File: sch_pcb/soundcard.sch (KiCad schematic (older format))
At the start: 52 parts, among them J501 MicroUSB, U501 CM108B, U502 CM108B, U503 TUSB2036, Y501 6MHz

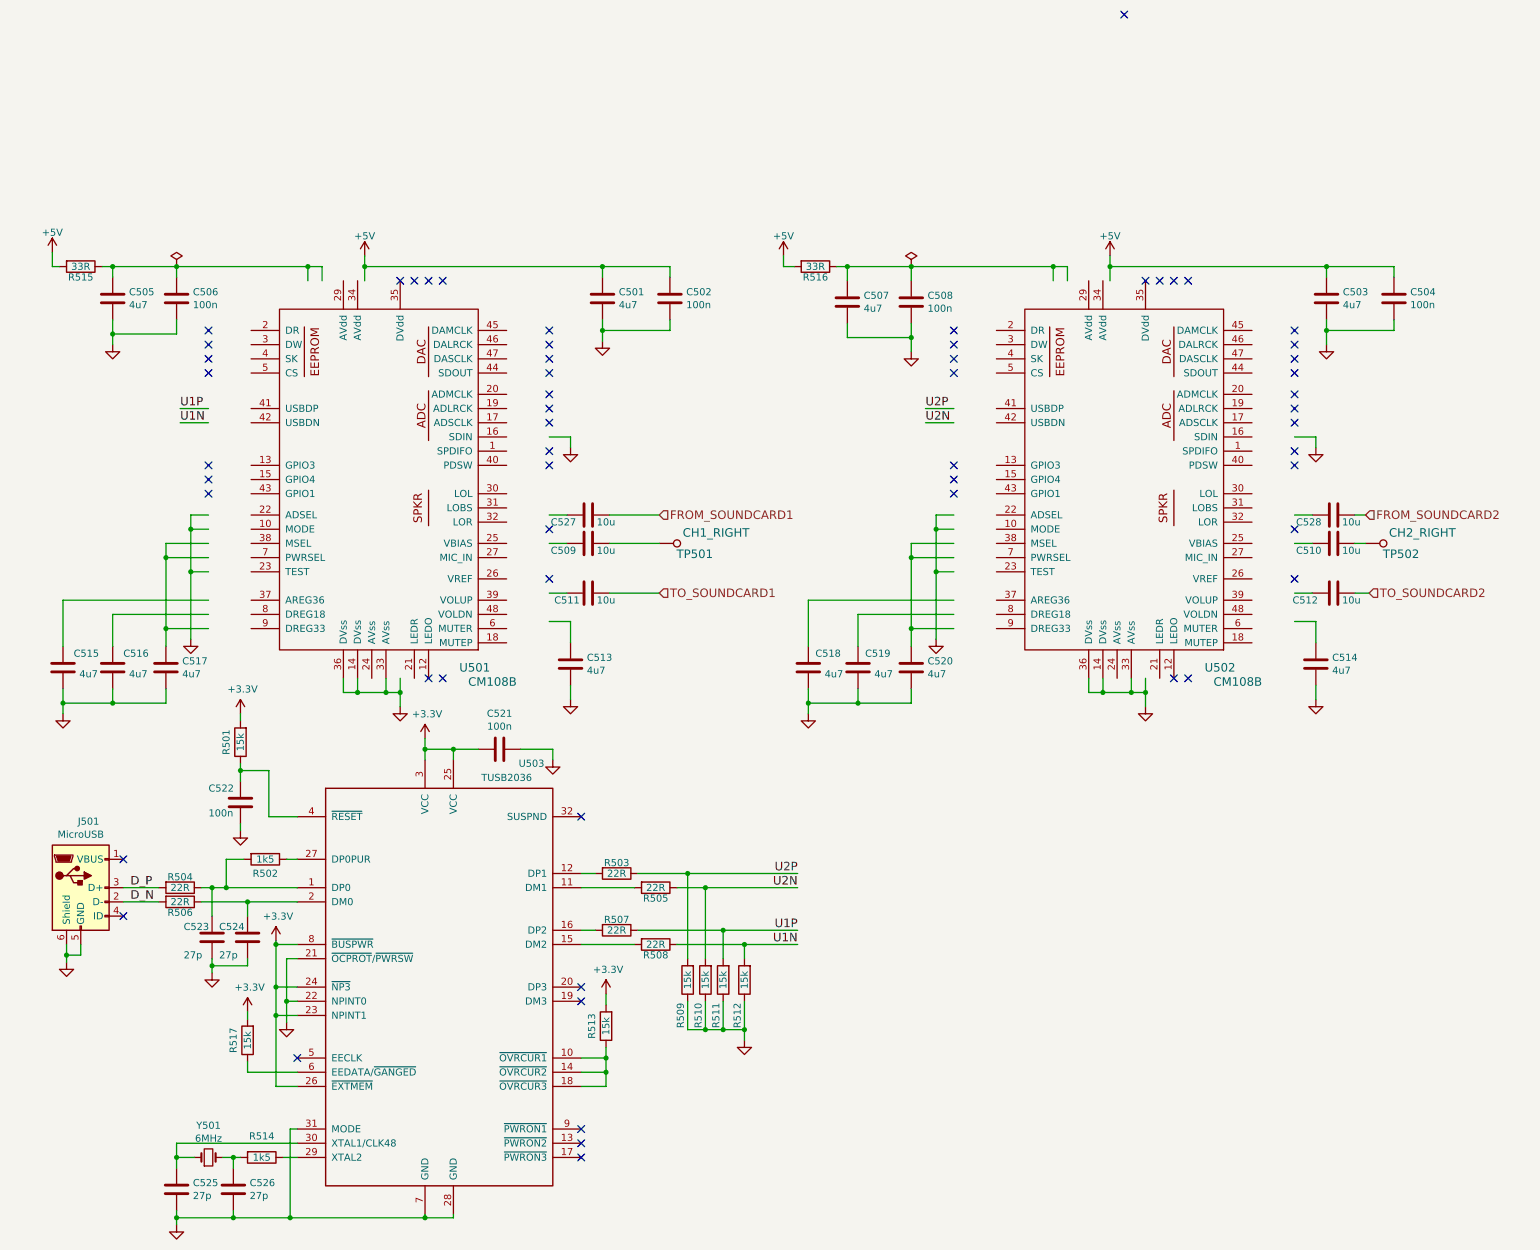
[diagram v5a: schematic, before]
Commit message: Add files via upload
Add a PMOS switch to allow turning on the soundcard section (hub and 2 soundcard chips) after the Pi has booted.  For some reason, doing so before the desktop loads causes it to hang..
Change gain resistors in opamp stages to move the sweet spot closer to the center of the digital pots to allow for more adjustment range
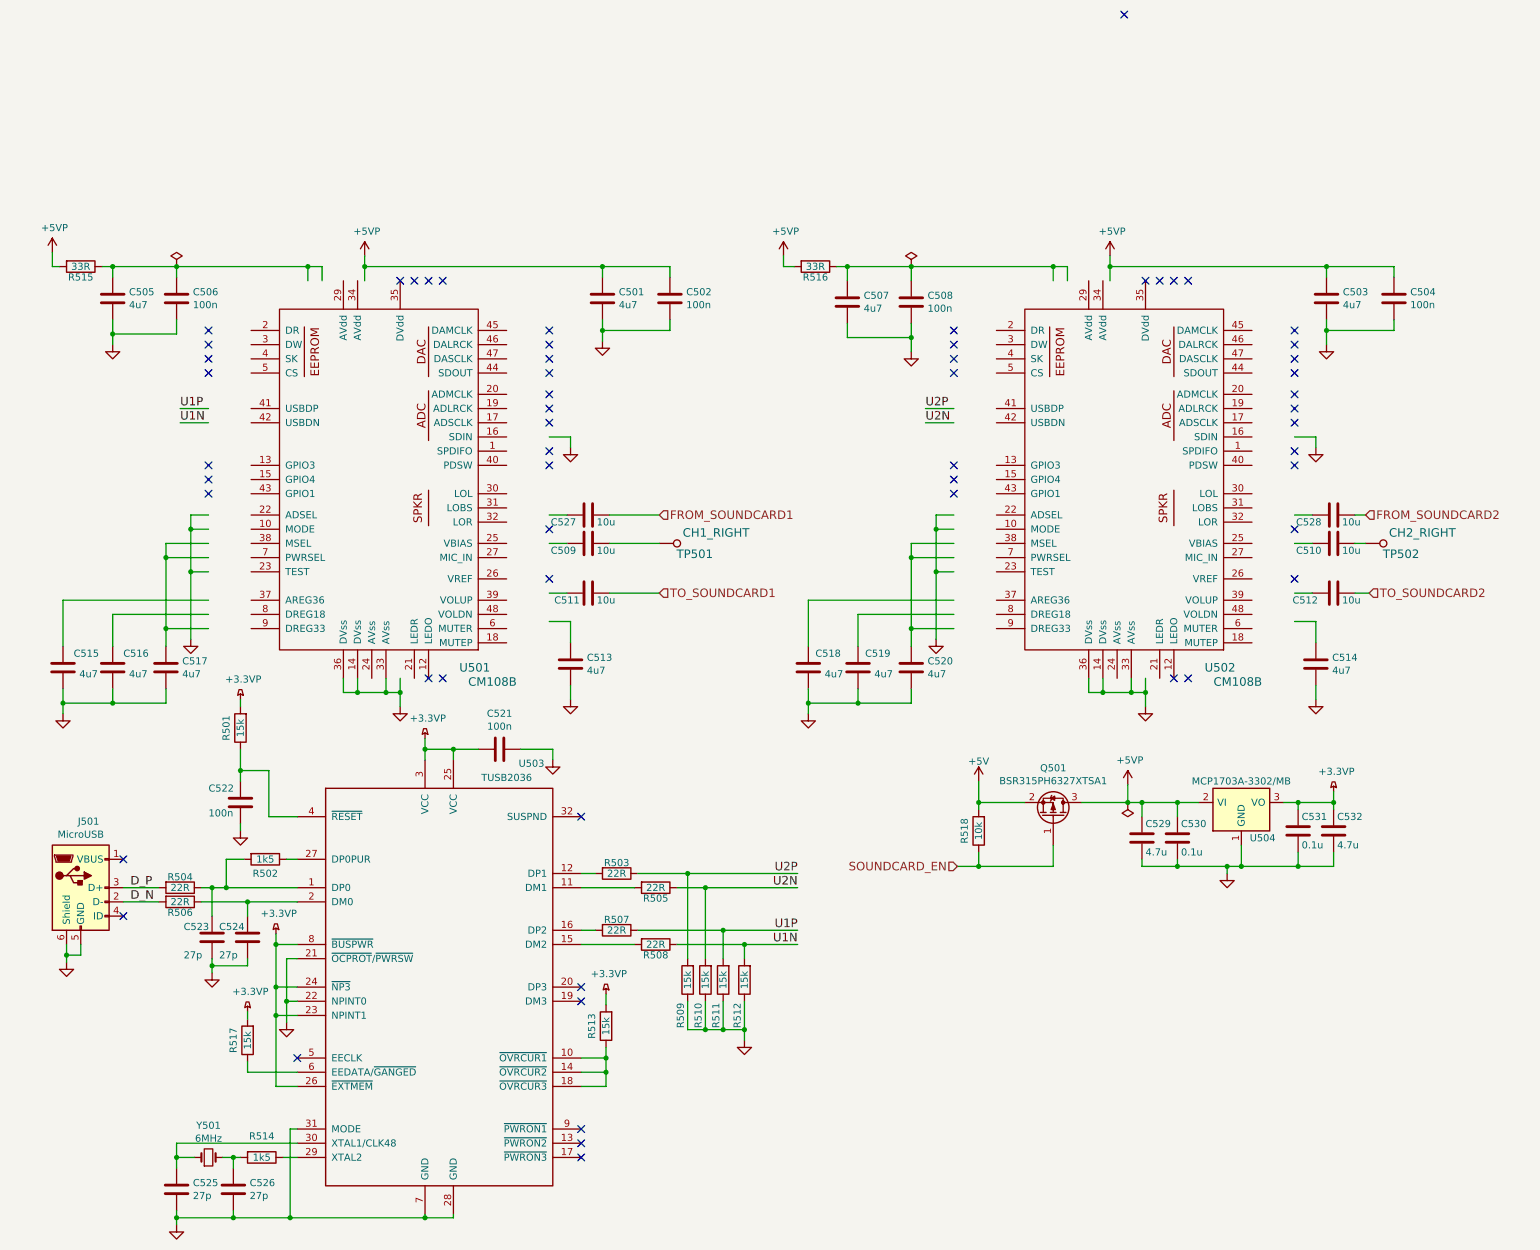
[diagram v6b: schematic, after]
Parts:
- added C529, C532: 4.7u, lib:smd0603, symbol C
- added C530, C531: 0.1u, lib:smd0603, symbol C
- added Q501: BSR315PH6327XTSA1, lib:SOT23, symbol BSS84
- added R518: 10k, lib:smd0603, symbol R
- added U504: MCP1703A-3302/MB, lib:sot89, symbol MCP1703A-2502/MB
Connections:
- net labels added: +3.3VP, +5VP, SOUNDCARD_EN
- net labels removed: +3.3V
- wire segments 174 -> 193
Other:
- moved on the sheet: R501

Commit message: Update board with third soundcard
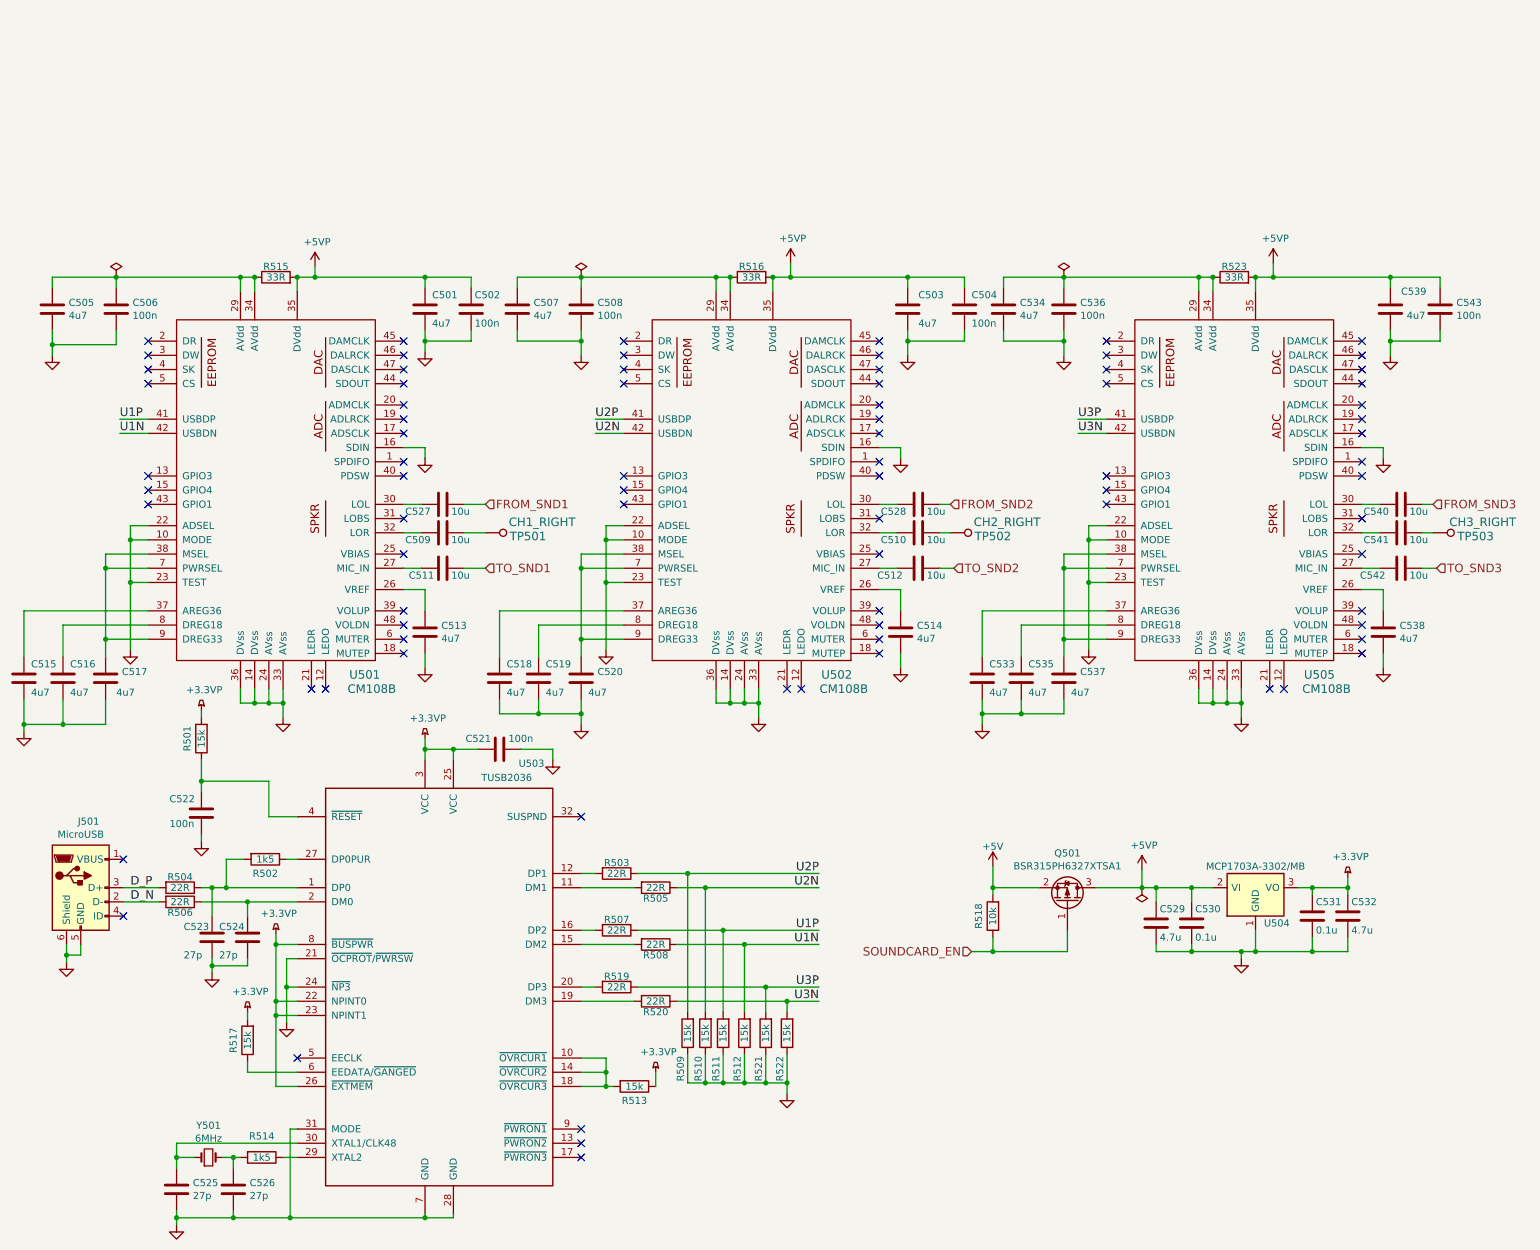
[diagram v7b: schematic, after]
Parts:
- added C533, C534, C535, C537, C538, C539: 4u7, lib:smd0603, symbol C
- added C536, C543: 100n, lib:smd0603, symbol C
- added C540, C541, C542: 10u, lib:smd0603, symbol C
- added R519, R520: 22R, lib:smd0603, symbol R
- added R521, R522: 15k, lib:smd0603, symbol R
- added R523: 33R, lib:smd0603, symbol R
- added TP503: CH3_RIGHT, lib:Wire_28AWG, symbol TESTPOINT
- added U505: CM108B, lib:LQFP-48_7x7mm_Pitch0.5mm, symbol CM108B
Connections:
- net labels added: FROM_SND1, FROM_SND2, FROM_SND3, TO_SND1, TO_SND2, TO_SND3, U3N, U3P
- net labels removed: FROM_SOUNDCARD1, FROM_SOUNDCARD2, TO_SOUNDCARD1, TO_SOUNDCARD2
- wire segments 193 -> 249
- no-connect marks 58 -> 79
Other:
- moved on the sheet: C501, C502, C503, C504, C505, C506, C507, C508, C509, C510, C511, C512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
